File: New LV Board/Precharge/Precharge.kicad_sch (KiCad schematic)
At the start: 27 parts, among them K1 G3VM-61G2, Q1 BSS214NW, Q2 MPSA42, Q4 IRLML5203, U1 LM2904, U3 NE555P, U4 LR8N3-G

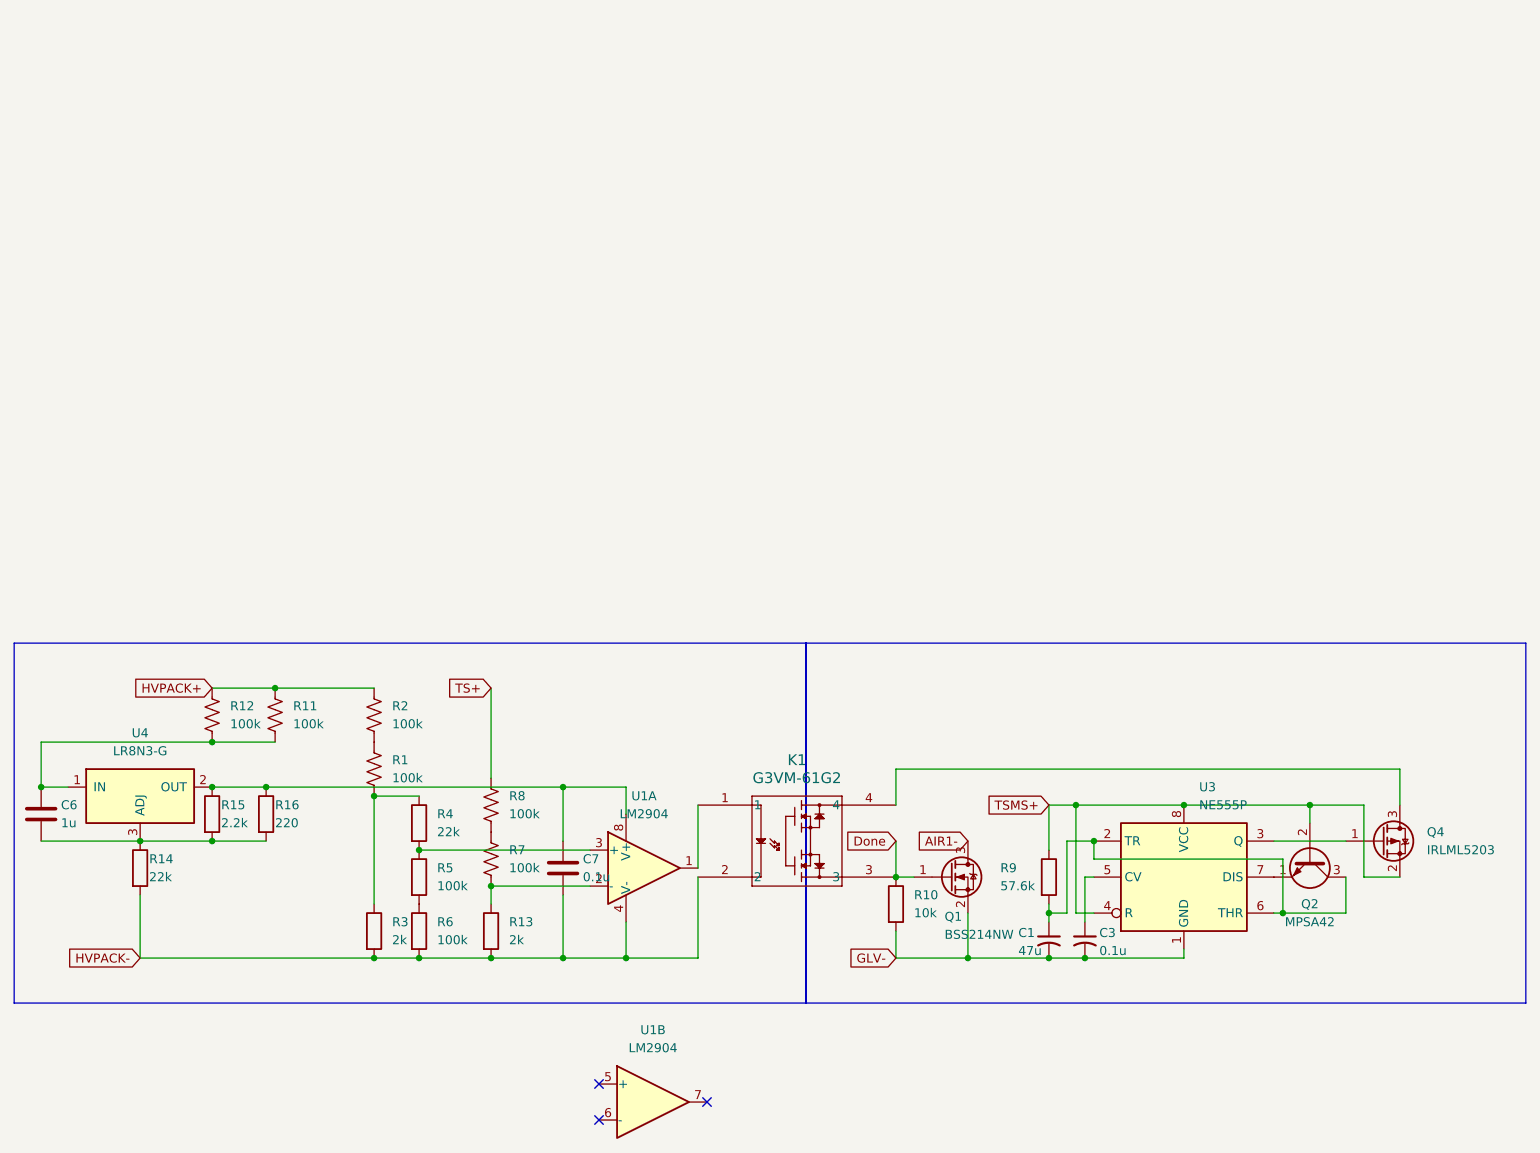
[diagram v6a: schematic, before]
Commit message: added screw terminals and GLV- trace
Haven't added any screw mount holes yet
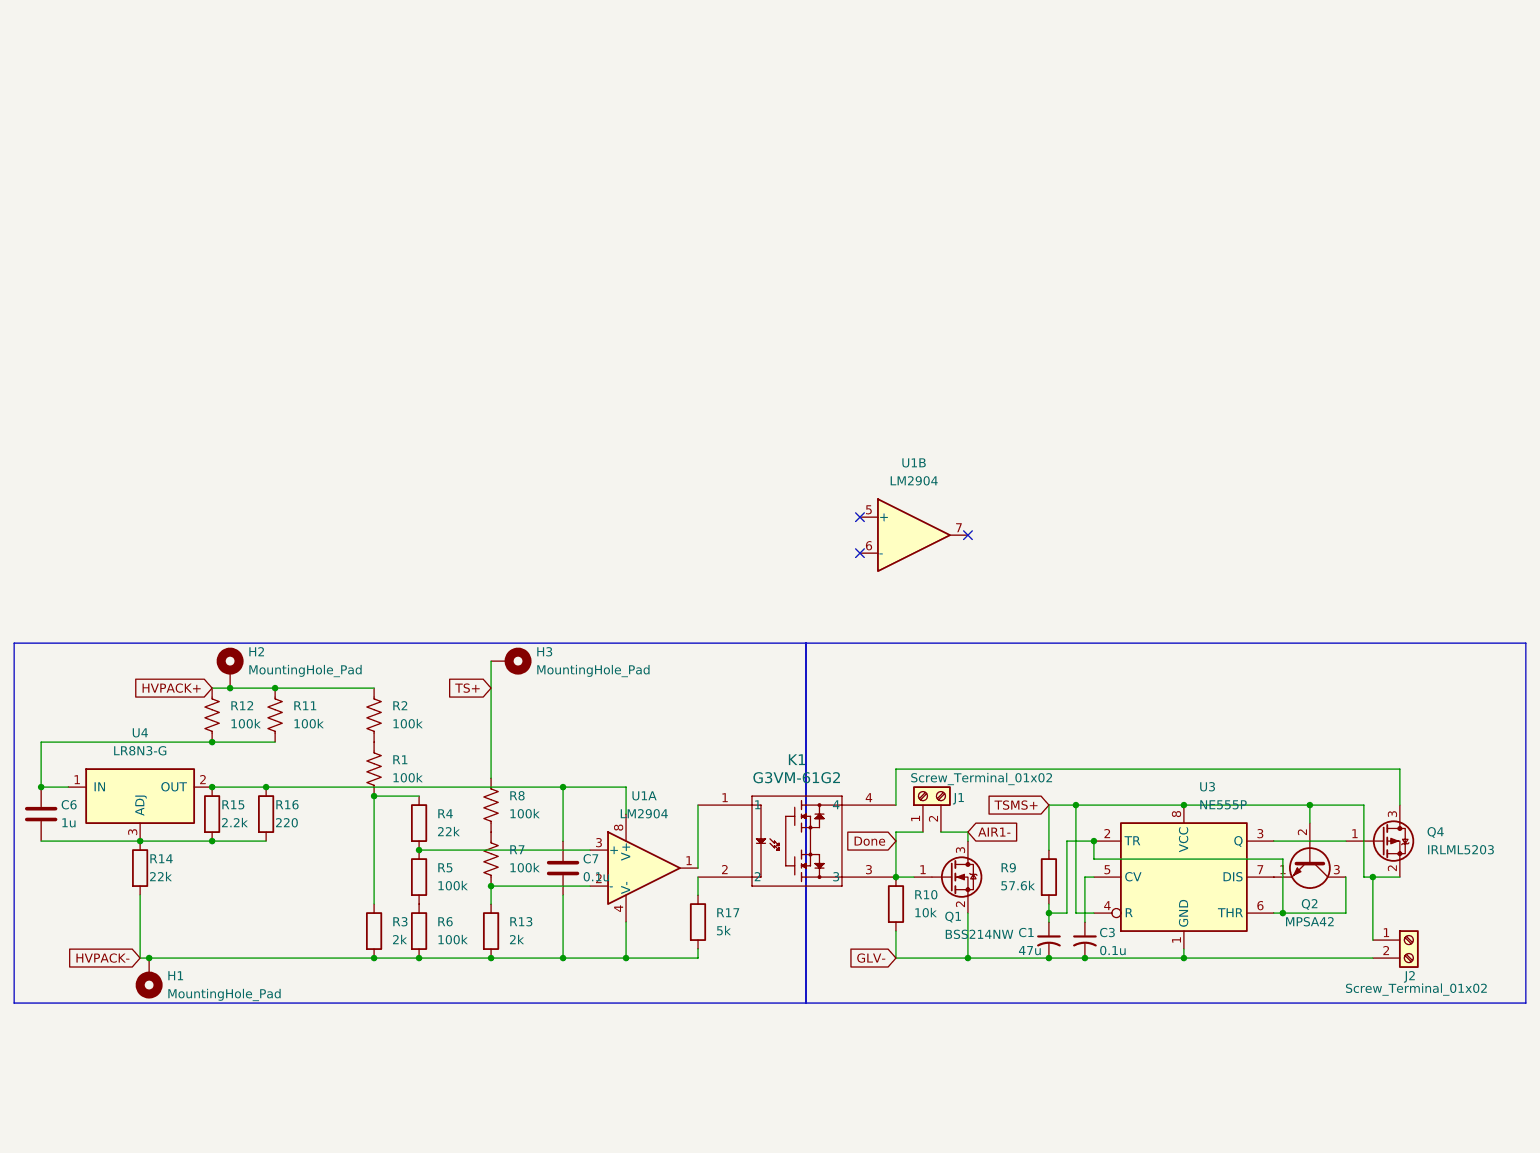
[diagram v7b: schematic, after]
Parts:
- added H1, H2, H3: MountingHole_Pad, symbol Mechanical:MountingHole_Pad
- added J1, J2: Screw_Terminal_01x02, TerminalBlock:TerminalBlock_MaiXu_MX126-5.0-02P_1x02_P5.00mm, symbol Connector:Screw_Terminal_01x02
- added R17: 5k, Resistor_THT:R_Axial_DIN0207_L6.3mm_D2.5mm_P2.54mm_Vertical, symbol Device:R
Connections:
- net AIR1-: now also J1.2 (Pin_2)
- net Done: now also J1.1 (Pin_1)
- net GLV-: now also J2.2 (Pin_2)
- net HVPACK+: now also H2.1
- net HVPACK-: now also H1.1, R17.2; no longer K1.2
- net TS+: now also H3.1
- net TSMS+: now also J2.1 (Pin_1)
- new net: K1.2, R17.1
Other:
- moved on the sheet: U1B

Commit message: added mounting holes
does HV- need to be traced?
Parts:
- H1, H2, H3: footprint (none) -> MountingHole:MountingHole_5.3mm_M5_DIN965_Pad; now in the parts list
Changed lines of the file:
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@@
 		(unit 1)
 		(exclude_from_sim no)
-		(in_bom no)
+		(in_bom yes)
 		(on_board yes)
 		(dnp no)
@@
 			)
 		)
-		(property "Footprint" ""
+		(property "Footprint" "MountingHole:MountingHole_5.3mm_M5_DIN965_Pad"
 			(at 36.83 153.67 0)
 			(effects
@@
 		(unit 1)
 		(exclude_from_sim no)
-		(in_bom no)
+		(in_bom yes)
 		(on_board yes)
 		(dnp no)
@@
 			)
 		)
-		(property "Footprint" ""
+		(property "Footprint" "MountingHole:MountingHole_5.3mm_M5_DIN965_Pad"
 			(at 87.63 109.22 0)
 			(effects
@@
 		(unit 1)
 		(exclude_from_sim no)
-		(in_bom no)
+		(in_bom yes)
 		(on_board yes)
 		(dnp no)
@@
 			)
 		)
-		(property "Footprint" ""
+		(property "Footprint" "MountingHole:MountingHole_5.3mm_M5_DIN965_Pad"
 			(at 48.26 110.49 0)
 			(effects
